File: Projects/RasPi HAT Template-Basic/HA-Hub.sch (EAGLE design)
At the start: 1 part, among them X1 RASPI_BOARD_B+_H

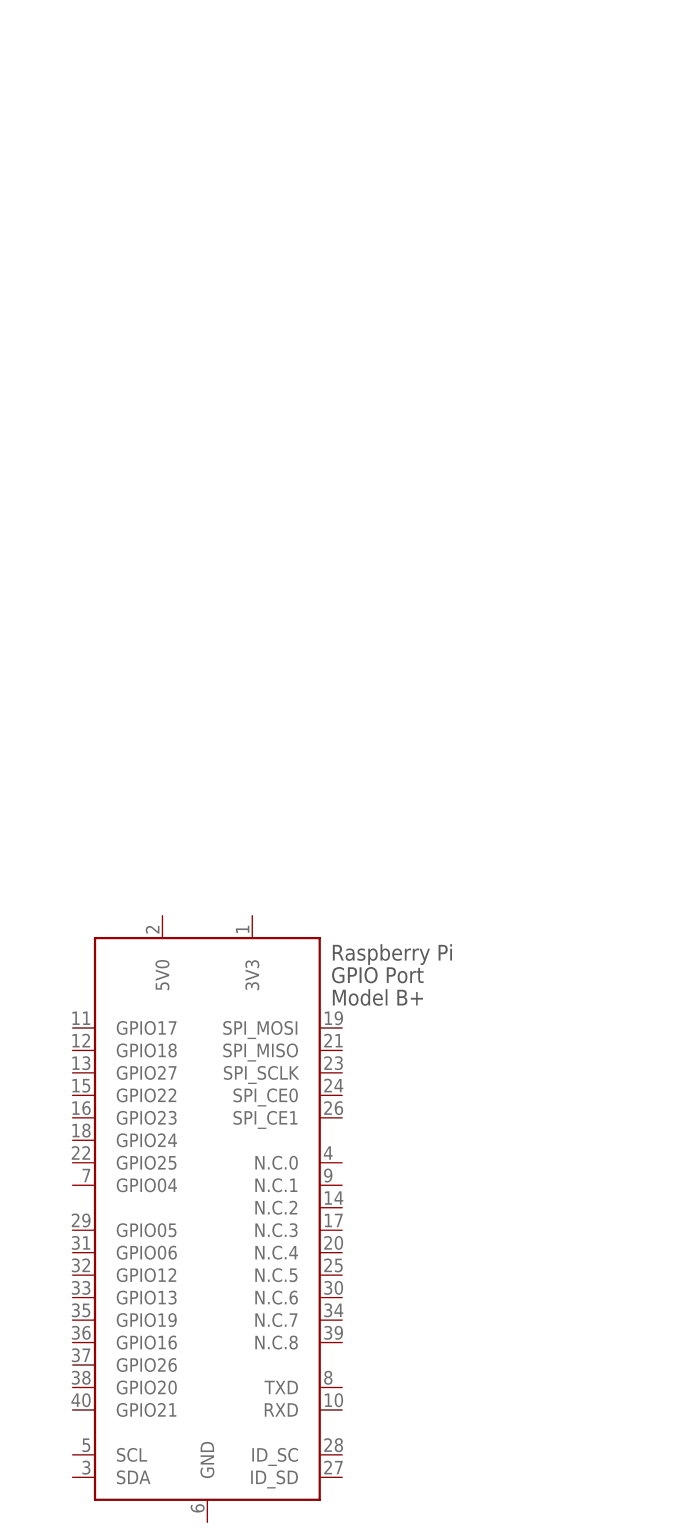
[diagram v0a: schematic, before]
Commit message: Changed v1.3 board 'via' drill size to 13mil. Plus some house keeping,
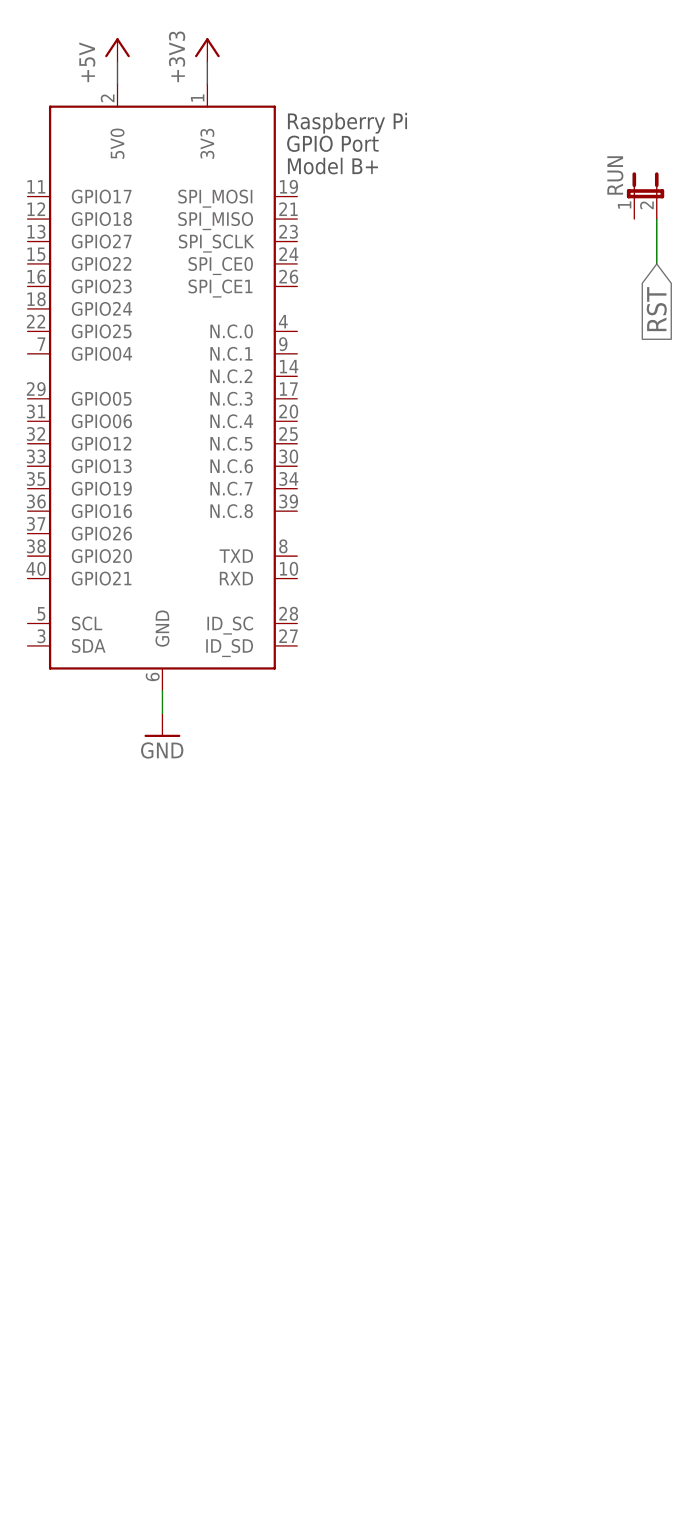
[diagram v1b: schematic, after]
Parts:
- added RUN: RST, jumper:JP1E
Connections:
- new net +3V3: X1.3V3
- new net +5V: X1.5V0
- new net GND: X1.GND
- new net RST: RUN.2
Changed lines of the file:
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@@
 <layer number="48" name="Document" color="7" fill="1" visible="no" active="no"/>
 <layer number="49" name="Reference" color="7" fill="1" visible="no" active="no"/>
+<layer number="50" name="dxf" color="7" fill="1" visible="no" active="no"/>
 <layer number="51" name="tDocu" color="7" fill="1" visible="no" active="no"/>
 <layer number="52" name="bDocu" color="7" fill="1" visible="no" active="no"/>
+<layer number="53" name="tGND_GNDA" color="7" fill="9" visible="no" active="no"/>
+<layer number="54" name="bGND_GNDA" color="1" fill="9" visible="no" active="no"/>
+<layer number="56" name="wert" color="7" fill="1" visible="no" active="no"/>
+<layer number="57" name="tCAD" color="7" fill="1" visible="no" active="no"/>
 <layer number="90" name="Modules" color="5" fill="1" visible="yes" active="yes"/>
 <layer number="91" name="Nets" color="2" fill="1" visible="yes" active="yes"/>
@@
 <layer number="97" name="Info" color="7" fill="1" visible="yes" active="yes"/>
 <layer number="98" name="Guide" color="6" fill="1" visible="yes" active="yes"/>
+<layer number="99" name="SpiceOrder" color="7" fill="1" visible="no" active="no"/>
+<layer number="100" name="Muster" color="7" fill="1" visible="no" active="no"/>
+<layer number="101" name="Patch_Top" color="12" fill="4" visible="no" active="yes"/>
+<layer number="102" name="Vscore" color="7" fill="1" visible="no" active="yes"/>
+<layer number="103" name="fp3" color="7" fill="1" visible="no" active="yes"/>
+<layer number="104" name="Name" color="7" fill="1" visible="no" active="yes"/>
+<layer number="105" name="Beschreib" color="9" fill="1" visible="no" active="yes"/>
+<layer number="106" name="BGA-Top" color="4" fill="1" visible="no" active="yes"/>
+<layer number="107" name="BD-Top" color="5" fill="1" visible="no" active="yes"/>
+<layer number="108" name="fp8" color="7" fill="1" visible="no" active="yes"/>
+<layer number="109" name="fp9" color="7" fill="1" visible="no" active="yes"/>
+<layer number="110" name="fp0" color="7" fill="1" visible="no" active="yes"/>
+<layer number="111" name="LPC17xx" color="7" fill="1" visible="no" active="yes"/>
+<layer number="112" name="tSilk" color="7" fill="1" visible="no" active="yes"/>
+<layer number="113" name="ReferenceLS" color="7" fill="1" visible="no" active="no"/>
+<layer number="116" name="Patch_BOT" color="9" fill="4" visible="no" active="yes"/>
+<layer number="118" name="Rect_Pads" color="7" fill="1" visible="no" active="no"/>
+<layer number="121" name="_tsilk" color="7" fill="1" visible="no" active="yes"/>
+<layer number="122" name="_bsilk" color="7" fill="1" visible="no" active="yes"/>
+<layer number="123" name="tTestmark" color="7" fill="1" visible="no" active="yes"/>
+<layer number="124" name="bTestmark" color="7" fill="1" visible="no" active="yes"/>
+<layer number="125" name="_tNames" color="7" fill="1" visible="no" active="yes"/>
+<layer number="126" name="_bNames" color="7" fill="1" visible="no" active="yes"/>
+<layer number="127" name="_tValues" color="7" fill="1" visible="no" active="yes"/>
+<layer number="128" name="_bValues" color="7" fill="1" visible="no" active="yes"/>
+<layer number="131" name="tAdjust" color="7" fill="1" visible="no" active="yes"/>
+<layer number="132" name="bAdjust" color="7" fill="1" visible="no" active="yes"/>
+<layer number="144" name="Drill_legend" color="7" fill="1" visible="no" active="yes"/>
+<layer number="150" name="Notes" color="7" fill="1" visible="no" active="yes"/>
+<layer number="151" name="HeatSink" color="7" fill="1" visible="no" active="yes"/>
+<layer number="152" name="_bDocu" color="7" fill="1" visible="no" active="yes"/>
+<layer number="153" name="FabDoc1" color="6" fill="1" visible="no" active="no"/>
+<layer number="154" name="FabDoc2" color="2" fill="1" visible="no" active="no"/>
+<layer number="155" name="FabDoc3" color="7" fill="15" visible="no" active="no"/>
+<layer number="199" name="Contour" color="7" fill="1" visible="no" active="yes"/>
+<layer number="200" name="200bmp" color="1" fill="10" visible="no" active="yes"/>
+<layer number="201" name="201bmp" color="2" fill="1" visible="no" active="no"/>
+<layer number="202" name="202bmp" color="3" fill="1" visible="no" active="no"/>
+<layer number="203" name="203bmp" color="4" fill="10" visible="no" active="yes"/>
+<layer number="204" name="204bmp" color="5" fill="10" visible="no" active="yes"/>
+<layer number="205" name="205bmp" color="6" fill="10" visible="no" active="yes"/>
+<layer number="206" name="206bmp" color="7" fill="10" visible="no" active="yes"/>
+<layer number="207" name="207bmp" color="8" fill="10" visible="no" active="yes"/>
+<layer number="208" name="208bmp" color="9" fill="10" visible="no" active="yes"/>
+<layer number="209" name="209bmp" color="7" fill="1" visible="no" active="yes"/>
+<layer number="210" name="210bmp" color="7" fill="1" visible="no" active="yes"/>
+<layer number="211" name="211bmp" color="7" fill="1" visible="no" active="yes"/>
+<layer number="212" name="212bmp" color="7" fill="1" visible="no" active="yes"/>
+<layer number="213" name="213bmp" color="7" fill="1" visible="no" active="yes"/>
+<layer number="214" name="214bmp" color="7" fill="1" visible="no" active="yes"/>
+<layer number="215" name="215bmp" color="7" fill="1" visible="no" active="yes"/>
+<layer number="216" name="216bmp" color="7" fill="1" visible="no" active="yes"/>
+<layer number="217" name="217bmp" color="18" fill="1" visible="no" active="no"/>
+<layer number="218" name="218bmp" color="19" fill="1" visible="no" active="no"/>
+<layer number="219" name="219bmp" color="20" fill="1" visible="no" active="no"/>
+<layer number="220" name="220bmp" color="21" fill="1" visible="no" active="no"/>
+<layer number="221" name="221bmp" color="22" fill="1" visible="no" active="no"/>
+<layer number="222" name="222bmp" color="23" fill="1" visible="no" active="no"/>
+<layer number="223" name="223bmp" color="24" fill="1" visible="no" active="no"/>
+<layer number="224" name="224bmp" color="25" fill="1" visible="no" active="no"/>
+<layer number="231" name="Eagle3D_PG1" color="7" fill="1" visible="no" active="no"/>
+<layer number="232" name="Eagle3D_PG2" color="7" fill="1" visible="no" active="no"/>
+<layer number="233" name="Eagle3D_PG3" color="7" fill="1" visible="no" active="no"/>
+<layer number="248" name="Housing" color="7" fill="1" visible="no" active="yes"/>
+<layer number="249" name="Edge" color="7" fill="1" visible="no" active="yes"/>
+<layer number="250" name="Descript" color="7" fill="1" visible="no" active="no"/>
+<layer number="251" name="SMDround" color="7" fill="1" visible="no" active="no"/>
+<layer number="254" name="cooling" color="7" fill="1" visible="no" active="yes"/>
 </layers>
 <schematic xreflabel="%F%N/%S.%C%R" xrefpart="/%S.%C%R">
@@
 <parts>
 <part name="X1" library="raspberrypi_bastelstube_v13" deviceset="RASPI_BOARD_B+" device="_H"/>
+<part name="P+2" library="supply1" deviceset="+5V" device=""/>
+<part name="+3V2" library="supply1" deviceset="+3V3" device=""/>
+<part name="GND2" library="supply1" deviceset="GND" device=""/>
+<part name="FRAME1" library="frames" deviceset="FRAME_B_L" device=""/>
+<part name="RUN" library="jumper" deviceset="JP1E" device="" value="RST">
+<attribute name="MF" value=""/>
+<attribute name="MPN" value="2211S-02G"/>
+<attribute name="OC_NEWARK" value="08N6744"/>
+</part>
 </parts>
 <sheets>
@@
 </plain>
 <instances>
-<instance part="X1" gate="G$1" x="58.42" y="124.46"/>
+<instance part="X1" gate="G$1" x="53.34" y="218.44"/>
+<instance part="P+2" gate="1" x="48.26" y="251.46"/>
+<instance part="+3V2" gate="G$1" x="58.42" y="251.46"/>
+<instance part="GND2" gate="1" x="53.34" y="172.72"/>
+<instance part="FRAME1" gate="G$1" x="0" y="0"/>
+<instance part="FRAME1" gate="G$2" x="325.12" y="0"/>
+<instance part="RUN" gate="A" x="106.68" y="233.68" smashed="yes">
+<attribute name="OC_NEWARK" x="106.68" y="233.68" size="1.016" layer="96" display="off"/>
+<attribute name="MF" x="106.68" y="233.68" size="1.016" layer="96" display="off"/>
+<attribute name="MPN" x="106.68" y="233.68" size="1.016" layer="96" display="off"/>
+<attribute name="NAME" x="105.41" y="233.68" size="1.778" layer="95" rot="R90"/>
+</instance>
 </instances>
 <busses>
 </busses>
 <nets>
+<net name="+3V3" class="0">
+<segment>
+<pinref part="X1" gate="G$1" pin="3V3"/>
+<pinref part="+3V2" gate="G$1" pin="+3V3"/>
+<wire x1="58.42" y1="248.92" x2="58.42" y2="246.38" width="0.1524" layer="91"/>
+</segment>
+</net>
+<net name="+5V" class="0">
+<segment>
+<pinref part="X1" gate="G$1" pin="5V0"/>
+<pinref part="P+2" gate="1" pin="+5V"/>
+<wire x1="48.26" y1="248.92" x2="48.26" y2="246.38" width="0.1524" layer="91"/>
+</segment>
+</net>
+<net name="GND" class="0">
+<segment>
+<pinref part="X1" gate="G$1" pin="GND"/>
+<pinref part="GND2" gate="1" pin="GND"/>
+<wire x1="53.34" y1="175.26" x2="53.34" y2="177.8" width="0.1524" layer="91"/>
+</segment>
+</net>
+<net name="RST" class="0">
+<segment>
+<label x="109.22" y="226.06" size="2.1844" layer="95" rot="R270" xref="yes"/>
+<wire x1="109.22" y1="231.14" x2="109.22" y2="226.06" width="0.1524" layer="91"/>
+<pinref part="RUN" gate="A" pin="2"/>
+</segment>
+</net>
 </nets>
 </sheet>
